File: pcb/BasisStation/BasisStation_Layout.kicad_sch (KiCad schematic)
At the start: 22 parts, among them J5 Conn_02x05_Odd_Even, J6 Conn_02x03_Odd_Even, Q1 BC337, Q2 BC337, Q3 BC337, Q4 BC337, U6 ESP32-S3-WROOM-1

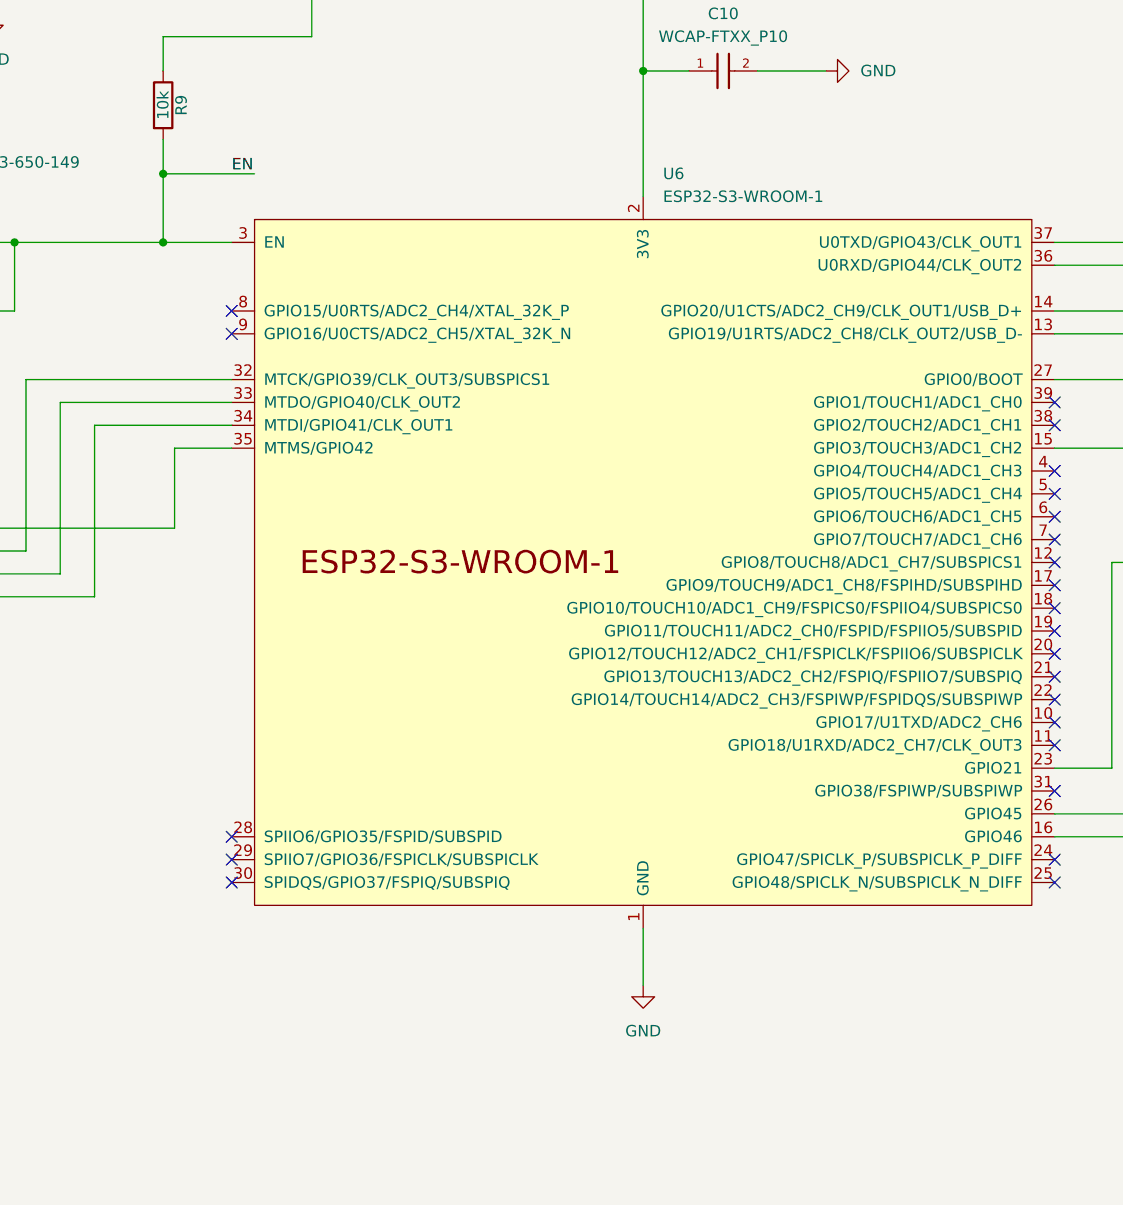
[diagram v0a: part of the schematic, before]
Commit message: v0.00.001 fix(SHBS-7): U6 auf ESP32-S3-WROOM-1U-N16R8-Symbol umgestellt
Espressif-Stil-Symbol in Bauteile-Bibliothek, sym-lib-table ergänzt.
Schaltplan, Netlist und PCB-Value für U6 auf N16R8 vereinheitlicht.
ERC ohne Fehler (ERC.rpt aktualisiert).

Co-authored-by: Cursor <cursoragent@cursor.com>
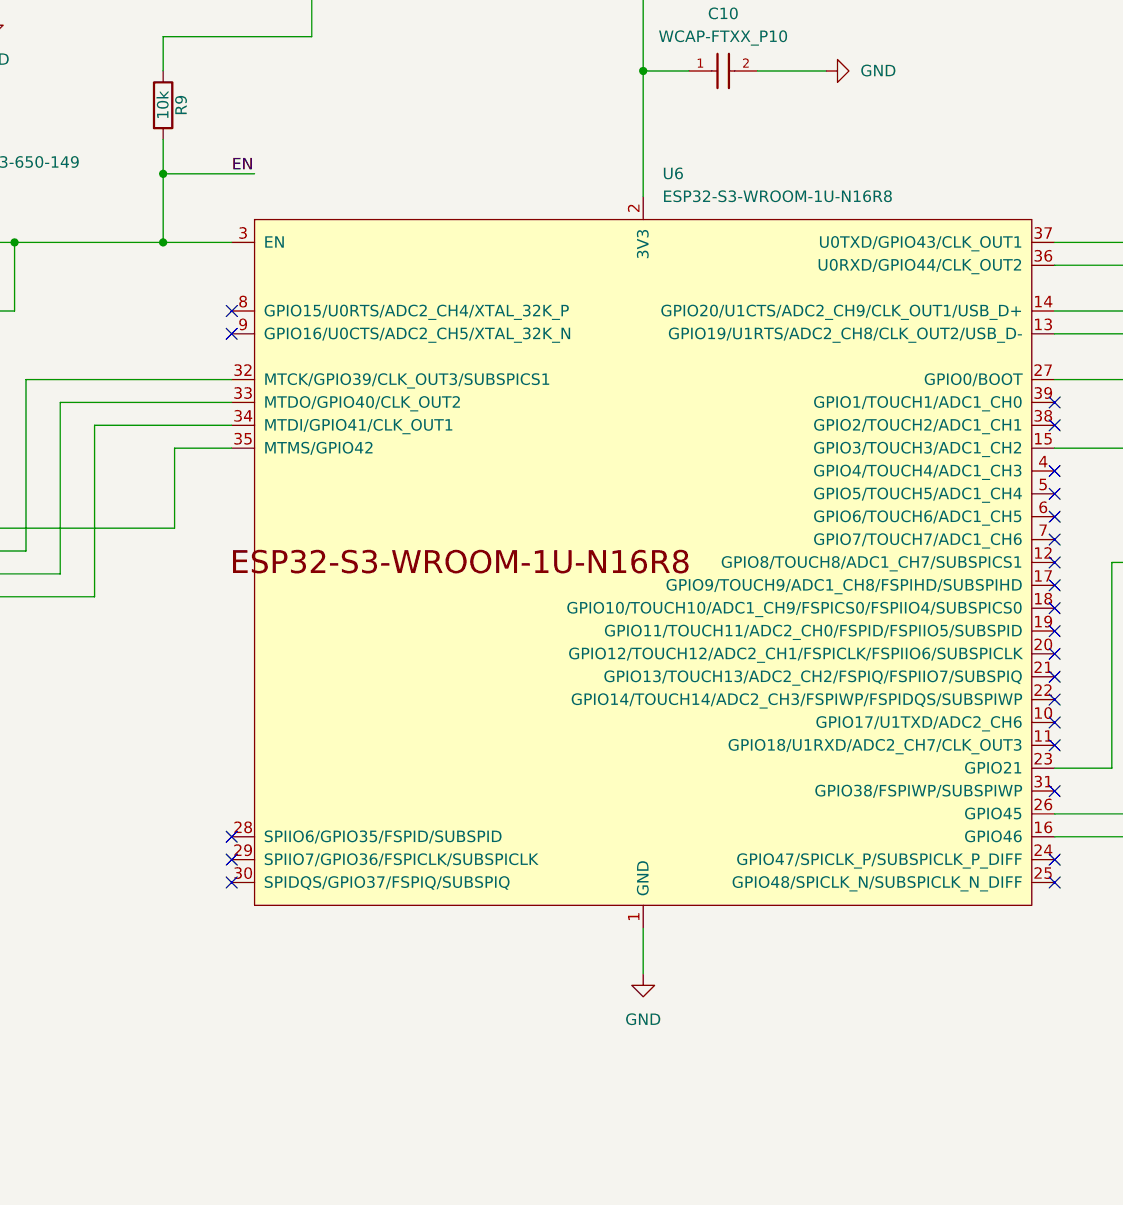
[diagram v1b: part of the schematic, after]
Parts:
- U6: value ESP32-S3-WROOM-1 -> ESP32-S3-WROOM-1U-N16R8; footprint Footprints:ESP32-S3-WROOM-1U -> RF_Module:ESP32-S3-WROOM-1U; symbol Espressif:ESP32-S3-WROOM-1 -> ESP32-S3-WROOM-1U-N16R8:ESP32-S3-WROOM-1U-N16R8; Height (none) -> 3.35; Manufacturer_Name (none) -> Espressif Systems; Manufacturer_Part_Number (none) -> ESP32-S3-WROOM-1U-N16R8; Mouser Part Number (none) -> 356-ESP32S3WM1UN16R8; Mouser Price/Stock (none) -> https://www.mouser.co.uk/ProductDetail/Espressif-Systems/ES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
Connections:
- net GND renamed EPAD
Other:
- moved on the sheet: U6
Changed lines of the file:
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@@
 	)
 	(no_connect
+		(at 92.71 127)
+	)
+	(no_connect
 		(at 184.15 88.9)
 	)
@@
 	)
 	(no_connect
-		(at 184.15 78.74)
+		(at 92.71 132.08)
 	)
 	(no_connect
-		(at 92.71 127)
+		(at 184.15 78.74)
 	)
 	(no_connect
@@
 	)
 	(no_connect
-		(at 92.71 132.08)
-	)
-	(no_connect
-		(at 92.71 129.54)
-	)
-	(no_connect
 		(at 184.15 129.54)
 	)
@@
 		(at 92.71 71.12)
 	)
+	(no_connect
+		(at 92.71 129.54)
+	)
 	(wire
 		(pts
@@
 	(wire
 		(pts
-			(xy 138.43 137.16) (xy 138.43 143.51)
-		)
-		(stroke
-			(width 0)
-			(type default)
-		)
-	)
-	(wire
-		(pts
 			(xy 101.6 22.86) (xy 138.43 22.86)
 		)
@@
 	(wire
 		(pts
+			(xy 138.43 137.16) (xy 138.43 142.24)
+		)
+		(stroke
+			(width 0)
+			(type default)
+		)
+	)
+	(wire
+		(pts
 			(xy 257.81 116.84) (xy 270.51 116.84)
 		)
@@
 	)
 	(symbol
-		(lib_id "Espressif:ESP32-S3-WROOM-1")
+		(lib_id "ESP32-S3-WROOM-1U-N16R8:ESP32-S3-WROOM-1U-N16R8")
 		(at 138.43 96.52 0)
 		(unit 1)
@@
 		(fields_autoplaced yes)
 		(property "Reference" "U6"
-			(at 140.6241 53.34 0)
+			(at 140.5733 53.34 0)
 			(effects
 				(font
@@
 			)
 		)
-		(property "Value" "ESP32-S3-WROOM-1"
-			(at 140.6241 55.88 0)
+		(property "Value" "ESP32-S3-WROOM-1U-N16R8"
+			(at 140.5733 55.88 0)
 			(effects
 				(font
@@
 			)
 		)
-		(property "Footprint" "Footprints:ESP32-S3-WROOM-1U"
+		(property "Footprint" "RF_Module:ESP32-S3-WROOM-1U"
 			(at 140.97 144.78 0)
 			(effects
@@
 			)
 		)
-		(property "Description" "2.4 GHz WiFi (802.11 b/g/n) and Bluetooth ® 5 (LE) module Built around ESP32S3 series of SoCs, Xtensa ® dualcore 32bit LX7 microprocessor Flash up to 16 MB, PSRAM up to 8 MB 36 GPIOs, rich set of peripherals Onboard PCB antenna"
+		(property "Description" "ESP32-S3-WROOM-1U-N16R8: 16 MB flash, 8 MB octal PSRAM, IPEX antenna connector"
 			(at 138.43 96.52 0)
 			(effects
@@
 			)
 		)
+		(property "Height" "3.35"
+			(at 167.64 491.44 0)
+			(effects
+				(font
+					(size 1.27 1.27)
+				)
+				(justify left top)
+				(hide yes)
+			)
+		)
+		(property "Mouser Part Number" "356-ESP32S3WM1UN16R8"
+			(at 167.64 591.44 0)
+			(effects
+				(font
+					(size 1.27 1.27)
+				)
+				(justify left top)
+				(hide yes)
+			)
+		)
+		(property "Mouser Price/Stock" "https://www.mouser.co.uk/ProductDetail/Espressif-Systems/ESP32-S3-WROOM-1U-N16R8?qs=Li%252BoUPsLEns6V0Pr5KRJtw%3D%3D"
+			(at 167.64 691.44 0)
+			(effects
+				(font
+					(size 1.27 1.27)
+				)
+				(justify left top)
+				(hide yes)
+			)
+		)
+		(property "Manufacturer_Name" "Espressif Systems"
+			(at 167.64 791.44 0)
+			(effects
+				(font
+					(size 1.27 1.27)
+				)
+				(justify left top)
+				(hide yes)
+			)
+		)
+		(property "Manufacturer_Part_Number" "ESP32-S3-WROOM-1U-N16R8"
+			(at 167.64 891.44 0)
+			(effects
+				(font
+					(size 1.27 1.27)
+				)
+				(justify left top)
+				(hide yes)
+			)
+		)
 		(pin "38"
 		)
@@
 	(symbol
 		(lib_id "power:GND")
-		(at 138.43 143.51 0)
+		(at 138.43 142.24 0)
 		(unit 1)
 		(exclude_from_sim no)
@@
 		(fields_autoplaced yes)
 		(property "Reference" "#PWR037"
-			(at 138.43 149.86 0)
+			(at 138.43 148.59 0)
 			(effects
 				(font
@@
 		)
 		(property "Value" "GND"
-			(at 138.43 148.59 0)
+			(at 138.43 147.32 0)
 			(effects
 				(font
@@
 		)
 		(property "Footprint" ""
-			(at 138.43 143.51 0)
+			(at 138.43 142.24 0)
 			(effects
 				(font
@@
 		)
 		(property "Datasheet" ""
-			(at 138.43 143.51 0)
+			(at 138.43 142.24 0)
 			(effects
 				(font
@@
 		)
 		(property "Description" "Power symbol creates a global label with name \"GND\" , ground"
-			(at 138.43 143.51 0)
+			(at 138.43 142.24 0)
 			(effects
 				(font

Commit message: v0.00.001 feat(SHBS-8): WLAN-Antenne ANT1/ANT2 als mechanische BOM-Einträge
Co-authored-by: Cursor <cursoragent@cursor.com>
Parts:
- added ANT1: CAB.6061, symbol mechanical:WLAN_Pigtail
- added ANT2: GW.20.5150, symbol mechanical:WLAN_Antenna
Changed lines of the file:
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@@
+		)
+	)
+	(text_box "WLAN RF (mechanical, not routed on PCB):\nU6 IPEX ←plug→ ANT1 pigtail ←SMA bulkhead→ enclosure\nANT2 antenna screws onto bulkhead (outside)"
+		(exclude_from_sim no)
+		(at 123.19 152.4 0)
+		(size 31.75 15.24)
+		(margins 0.9525 0.9525 0.9525 0.9525)
+		(stroke
+			(width 0)
+			(type solid)
+		)
+		(fill
+			(type none)
+		)
+		(effects
+			(font
+				(size 1.27 1.27)
+			)
+			(justify left top)
 		)
 	)
@@
 	)
 	(symbol
+		(lib_id "mechanical:WLAN_Antenna")
+		(at 168.91 143.51 0)
+		(unit 1)
+		(exclude_from_sim no)
+		(in_bom yes)
+		(on_board no)
+		(dnp no)
+		(fields_autoplaced yes)
+		(property "Reference" "ANT2"
+			(at 182.88 142.2399 0)
+			(effects
+				(font
+					(size 1.27 1.27)
+				)
+				(justify left)
+			)
+		)
+		(property "Value" "GW.20.5150"
+			(at 182.88 144.7799 0)
+			(effects
+				(font
+					(size 1.27 1.27)
+				)
+				(justify left)
+			)
+		)
+		(property "Footprint" ""
+			(at 168.91 143.51 0)
+			(effects
+				(font
+					(size 1.27 1.27)
+				)
+				(hide yes)
+			)
+		)
+		(property "Datasheet" ""
+			(at 168.91 143.51 0)
+			(effects
+				(font
+					(size 1.27 1.27)
+				)
+				(hide yes)
+			)
+		)
+		(property "Description" "2.4 GHz dipole antenna, RP-SMA male"
+			(at 168.91 143.51 0)
+			(effects
+				(font
+					(size 1.27 1.27)
+				)
+				(hide yes)
+			)
+		)
+		(property "Manufacturer" "Taoglas"
+			(at 168.91 143.51 0)
+			(effects
+				(font
+					(size 1.27 1.27)
+				)
+				(hide yes)
+			)
+		)
+		(property "Manufacturer_Part_Number" "GW.20.5150"
+			(at 168.91 143.51 0)
+			(effects
+				(font
+					(size 1.27 1.27)
+				)
+				(hide yes)
+			)
+		)
+		(property "Mouser Part Number" "742-GW.20.5150"
+			(at 168.91 143.51 0)
+			(effects
+				(font
+					(size 1.27 1.27)
+				)
+				(hide yes)
+			)
+		)
+		(property "Mouser Price/Stock" "https://www.mouser.de/ProductDetail/Taoglas/GW-20-5150"
+			(at 168.91 143.51 0)
+			(effects
+				(font
+					(size 1.27 1.27)
+				)
+				(hide yes)
+			)
+		)
+		(instances
+			(project ""
+				(path "/498c7092-55c1-4229-9f4b-13c6a8e7da47/1af2eb5e-14cd-443f-ae96-dbfda52b298f"
+					(reference "ANT2")
+					(unit 1)
+				)
+			)
+		)
+	)
+	(symbol
 		(lib_id "power:+12V")
 		(at 15.24 19.05 0)
@@
 					(unit 1)
 				)
+			)
+		)
+	)
+	(symbol
+		(lib_id "mechanical:WLAN_Pigtail")
+		(at 107.95 144.78 0)
+		(unit 1)
+		(exclude_from_sim no)
+		(in_bom yes)
+		(on_board no)
+		(dnp no)
+		(fields_autoplaced yes)
+		(property "Reference" "ANT1"
+			(at 121.92 143.5099 0)
+			(effects
+				(font
+					(size 1.27 1.27)
+				)
+				(justify left)
+			)
+		)
+		(property "Value" "CAB.6061"
+			(at 121.92 146.0499 0)
+			(effects
+				(font
+					(size 1.27 1.27)
+				)
+				(justify left)
+			)
+		)
+		(property "Footprint" ""
+			(at 107.95 144.78 0)
+			(effects
+				(font
+					(size 1.27 1.27)
+				)
+				(hide yes)
+			)
+		)
+		(property "Datasheet" ""
+			(at 107.95 144.78 0)
+			(effects
+				(font
+					(size 1.27 1.27)
+				)
+				(hide yes)
+			)
+		)
+		(property "Description" "U.FL to RP-SMA female bulkhead, 100 mm"
+			(at 107.95 144.78 0)
+			(effects
+				(font
+					(size 1.27 1.27)
+				)
+				(hide yes)
+			)
+		)
+		(property "Manufacturer" "Taoglas"
+			(at 107.95 144.78 0)
+			(effects
+				(font
+					(size 1.27 1.27)
+				)
+				(hide yes)
+			)
+		)
+		(property "Manufacturer_Part_Number" "CAB.6061"
+			(at 107.95 144.78 0)
+			(effects
+				(font
+					(size 1.27 1.27)
+				)
+				(hide yes)
+			)
+		)
+		(property "Mouser Part Number" "742-CAB.6061"
+			(at 107.95 144.78 0)
+			(effects
+				(font
+					(size 1.27 1.27)
+				)
+				(hide yes)
+			)
+		)
+		(property "Mouser Price/Stock" "https://www.mouser.de/ProductDetail/Taoglas/CAB-6061"
+			(at 107.95 144.78 0)
+			(effects
+				(font
+					(size 1.27 1.27)
+				)
+				(hide yes)
+			)
+		)
+		(instances
+			(project ""
+				(path "/498c7092-55c1-4229-9f4b-13c6a8e7da47/1af2eb5e-14cd-443f-ae96-dbfda52b298f"
+					(reference "ANT1")
+					(unit 1)
+				)

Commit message: v0.00.001 feat(SHBS-4): USB-C-Stromversorgung mit MP2359-Buck auf 3,3V
PS2/+12V entfernt, neue Stromversorgungs-Schaltung (Stromversorgung.kicad_sch),
Footprints fuer MP2359DJ, SOT-23-6 und USB-C-Buchse, power_supply.md als
zentrale Referenz.

Co-Authored-By: Claude Sonnet 5 <noreply@anthropic.com>
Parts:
- removed PS2: TSR_1-2433E, Footprints:CONV_TSR_1-2433E, symbol TSR_1-2433E:TSR_1-2433E
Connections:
- net +3V3: no longer C10.1, C12.1, C8.1, J6.2 (Pin_2), R9.1, U6.2 (3V3)
- new net: C10.1, C12.1, J6.2 (Pin_2), R9.1, U6.2 (3V3)

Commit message: v0.00.001 fix(SHBS-4): +3V3 global verbunden, Symbolbibliothek entkoppelt
Die Projektbibliothek war in sym-lib-table unter dem Nickname "power"
registriert und verdeckte damit die gleichnamige KiCad-Standardbibliothek.
power:GND (28x), power:PWR_FLAG und power:+3V3 waren dadurch projektweit
nicht aufloesbar. Nickname auf "shbs_power" geaendert, lib_id von PS1 und
J_PWR1 samt ihrer lib_symbols-Cache-Eintraege nachgezogen. Alle uebrigen
power:*-Referenzen bleiben unveraendert und loesen jetzt gegen die
KiCad-Standardbibliothek auf.

Darauf aufbauend: +3V3 lag auf beiden Blaettern als lokales Label vor und
war damit blattlokal - der Buck-Ausgang erreichte U6 nicht (ERC
power_pin_not_driven an U6 Pin 2). Alle drei Vorkommen durch platzierte
power:+3V3-Symbole ersetzt (#PWR100 bis #PWR102).

Beide Schritte in einem Commit, weil power:+3V3 erst nach der Umbenennung
aufloesbar ist und die Aenderungen dieselbe Dateistelle betreffen.

ERC: 53 -> 29 Meldungen.

Co-Authored-By: Claude Opus 5 <noreply@anthropic.com>
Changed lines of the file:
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@@
 		)
 	)
-	(label "+3V3"
+	(symbol
+		(lib_id "power:+3V3")
 		(at 270.51 77.47 270)
-		(effects
-			(font
-				(size 1.27 1.27)
+		(unit 1)
+		(exclude_from_sim no)
+		(in_bom yes)
+		(on_board yes)
+		(dnp no)
+		(fields_autoplaced yes)
+		(property "Reference" "#PWR101"
+			(at 270.51 71.12 0)
+			(effects
+				(font
+					(size 1.27 1.27)
+				)
+				(hide yes)
 			)
-			(justify right bottom)
+		)
+		(property "Value" "+3V3"
+			(at 270.51 73.914 0)
+			(effects
+				(font
+					(size 1.27 1.27)
+				)
+			)
+		)
+		(property "Footprint" ""
+			(at 270.51 77.47 0)
+			(effects
+				(font
+					(size 1.27 1.27)
+				)
+				(hide yes)
+			)
+		)
+		(property "Datasheet" ""
+			(at 270.51 77.47 0)
+			(effects
+				(font
+					(size 1.27 1.27)
+				)
+				(hide yes)
+			)
+		)
+		(property "Description" "Power symbol creates a global label with name \"+3V3\""
+			(at 270.51 77.47 0)
+			(effects
+				(font
+					(size 1.27 1.27)
+				)
+				(hide yes)
+			)
+		)
+		(pin "1"
+		)
+		(instances
+			(project "BasisStation"
+				(path "/498c7092-55c1-4229-9f4b-13c6a8e7da47/1af2eb5e-14cd-443f-ae96-dbfda52b298f"
+					(reference "#PWR101")
+					(unit 1)
+				)
+			)
 		)
 	)
@@
 		)
 	)
-	(label "+3V3"
+	(symbol
+		(lib_id "power:+3V3")
 		(at 34.29 92.71 0)
-		(effects
-			(font
-				(size 1.27 1.27)
+		(unit 1)
+		(exclude_from_sim no)
+		(in_bom yes)
+		(on_board yes)
+		(dnp no)
+		(fields_autoplaced yes)
+		(property "Reference" "#PWR102"
+			(at 34.29 86.36 0)
+			(effects
+				(font
+					(size 1.27 1.27)
+				)
+				(hide yes)
 			)
-			(justify left bottom)
+		)
+		(property "Value" "+3V3"
+			(at 34.29 89.154 0)
+			(effects
+				(font
+					(size 1.27 1.27)
+				)
+			)
+		)
+		(property "Footprint" ""
+			(at 34.29 92.71 0)
+			(effects
+				(font
+					(size 1.27 1.27)
+				)
+				(hide yes)
+			)
+		)
+		(property "Datasheet" ""
+			(at 34.29 92.71 0)
+			(effects
+				(font
+					(size 1.27 1.27)
+				)
+				(hide yes)
+			)
+		)
+		(property "Description" "Power symbol creates a global label with name \"+3V3\""
+			(at 34.29 92.71 0)
+			(effects
+				(font
+					(size 1.27 1.27)
+				)
+				(hide yes)
+			)
+		)
+		(pin "1"
+		)
+		(instances
+			(project "BasisStation"
+				(path "/498c7092-55c1-4229-9f4b-13c6a8e7da47/1af2eb5e-14cd-443f-ae96-dbfda52b298f"
+					(reference "#PWR102")
+					(unit 1)
+				)
+			)
 		)
 	)

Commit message: v0.00.001 fix(SHBS-4): C8 Pin 1 an 3,3-V-Netz angeschlossen
C8 Pin 1 liegt bei (66,04 / 25,40), der zugehoerige Draht endete bei
(66,04 / 22,86) - ein Rasterversatz von exakt 2,54 mm (100 mil). Der
Stuetzkondensator war damit nicht angeschlossen (ERC: pin_not_connected
an C8 Pin 1, zusaetzlich unconnected_wire_endpoint).

Drahtsegment (66,04 / 22,86) -> (66,04 / 25,40) ergaenzt. C8 Pin 1 liegt
jetzt im 3,3-V-Netz von U6 (mit C10, C12, J6, R9).

Co-Authored-By: Claude Opus 5 <noreply@anthropic.com>
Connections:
- net at C10.1, C12.1, J6.2 (Pin_2)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: now also C8.1
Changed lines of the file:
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@@
+	(wire
+		(pts
+			(xy 66.04 22.86) (xy 66.04 25.4)
+		)
+		(stroke
+			(width 0)
+			(type default)
+		)
+	)
 	(wire
 		(pts
